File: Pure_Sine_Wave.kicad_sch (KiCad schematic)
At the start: 246 parts, among them J1 SOLAR, J10 Conn_01x01_Female, J11 Conn_01x01_Female, J12 Conn_01x01_Female, J13 Conn_01x01_Female, J14 Conn_01x01_Female, J15 Conn_01x01_Female, J16 Conn_01x01_Female, J17 Conn_01x01_Female, J18 Conn_01x01_Female, J19 Conn_01x01_Female, J2 Conn_01x01_Female, J20 Conn_01x01_Female, J21 Conn_01x01_Female, J22 Conn_01x01_Female, J23 Conn_01x01_Female, J24 Conn_01x01_Female, J25 Conn_01x01_Female, J26 Conn_01x01_Female, J27 Conn_01x01_Female, J28 Conn_01x01_Female, J29 Conn_01x01_Female, J3 Conn_01x01_Female, J30 Conn_01x01_Female, J31 Conn_01x01_Female, J32 Conn_01x01_Female, J33 Conn_01x01_Female, J34 Conn_01x01_Female, J36 FAN, J38 I2C_CON, J4 Conn_01x01_Female, J5 Conn_01x01_Female, J6 Conn_01x01_Female, J7 Conn_01x01_Female, J8 BATT, J9 USB_OTG, Q1 CSD19505, Q2 CSD19505, Q3 CSD19505, Q4 Si2306, Q5 2N3904, Q6 2N3904, Q7 PMOS-100V-78A, Q8 PMOS-100V-78A, Q9 Si2306, SW1 RIGHT, SW2 LEFT, SW3 BACK, SW4 SELECT, U1 ACS712-30A, U10 ADS1015, U11 NUP4202, U12 PCF8574, U2 B1212, U3 AMS1117-5.0, U4 AMS1117-3.3, U5 XL7005A, U6 XL7005A, U7 IR2104, U8 ESP32-WROOM-32, U9 CH340C

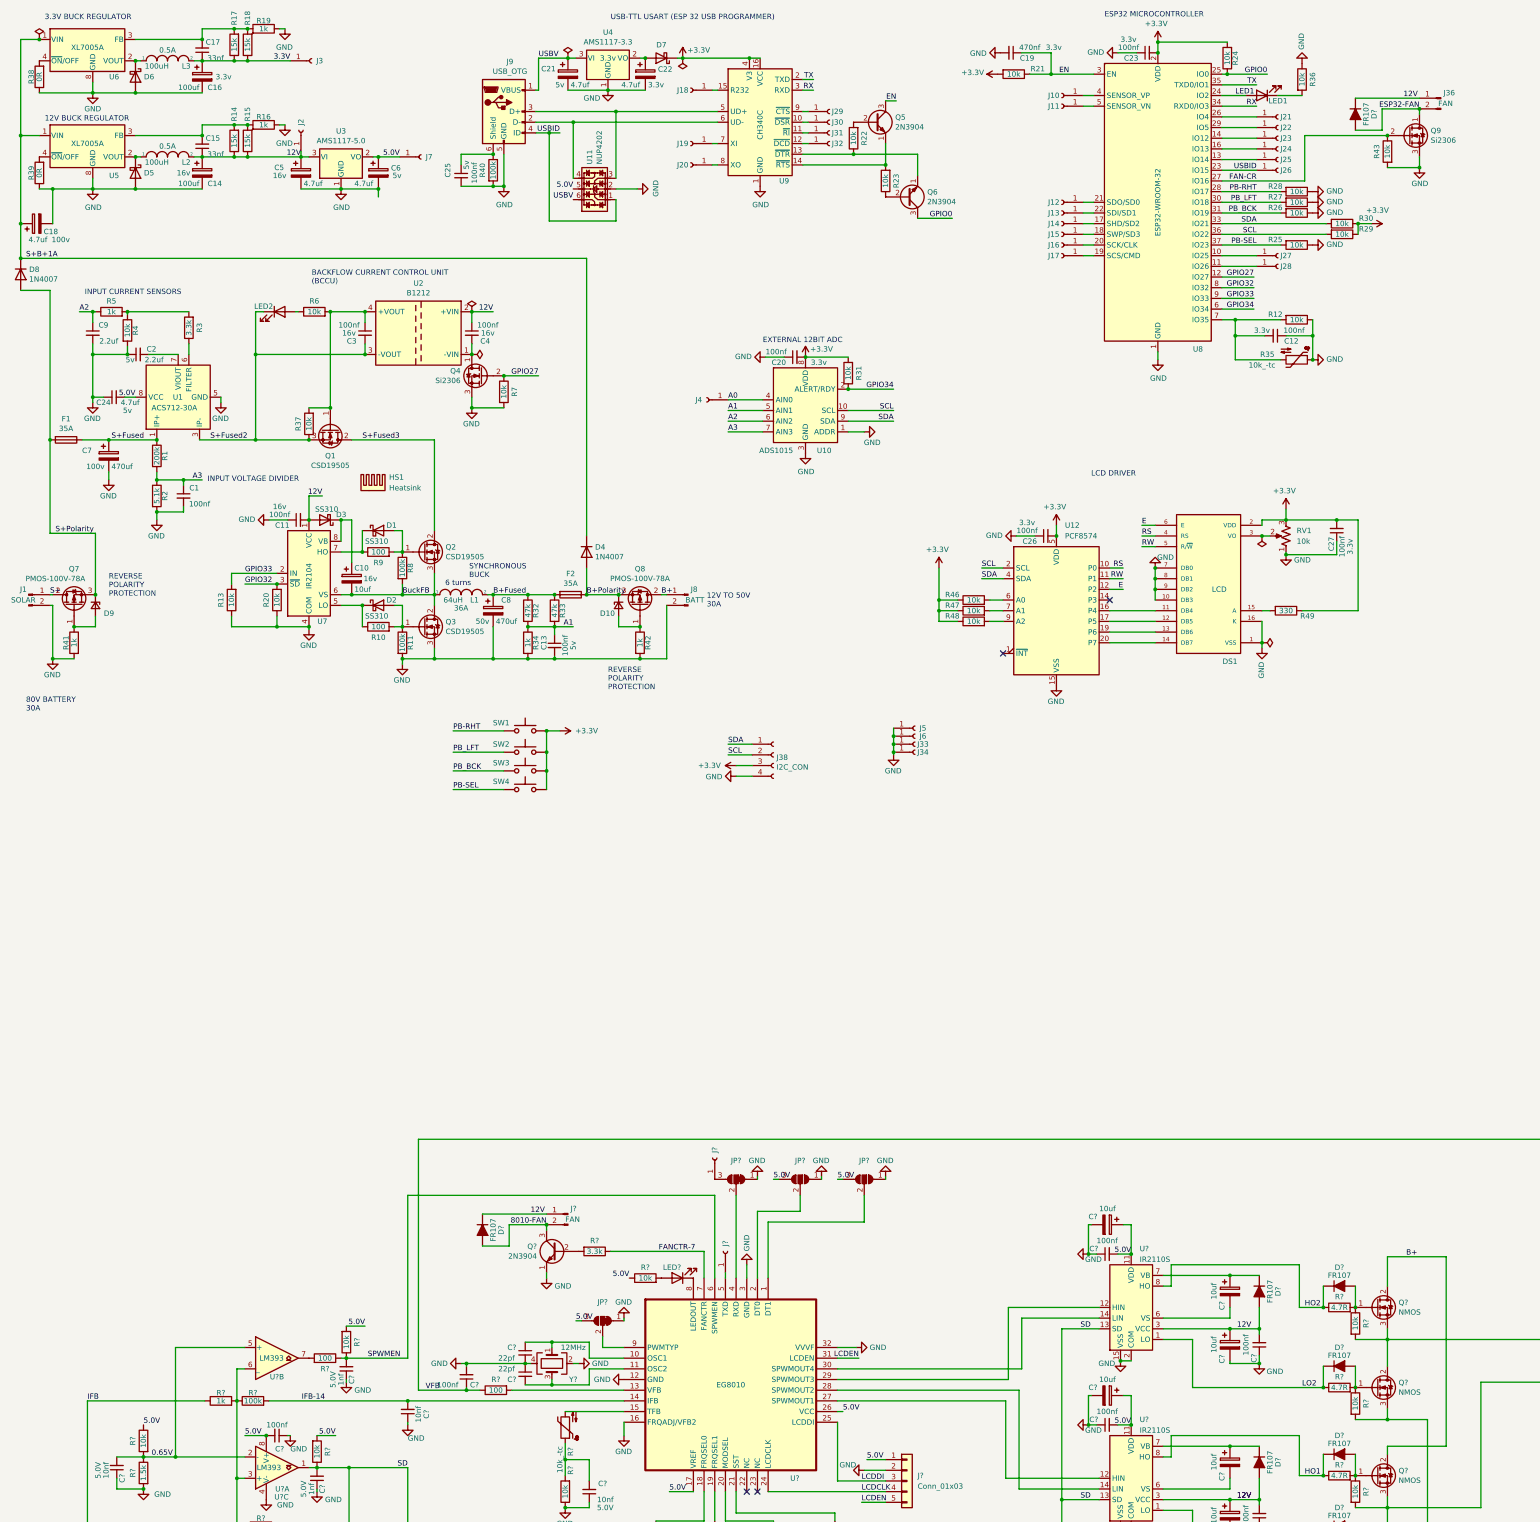
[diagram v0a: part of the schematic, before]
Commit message: Updated schematic to match changes form charge controller Added simulation for MOSFET heat predictions.
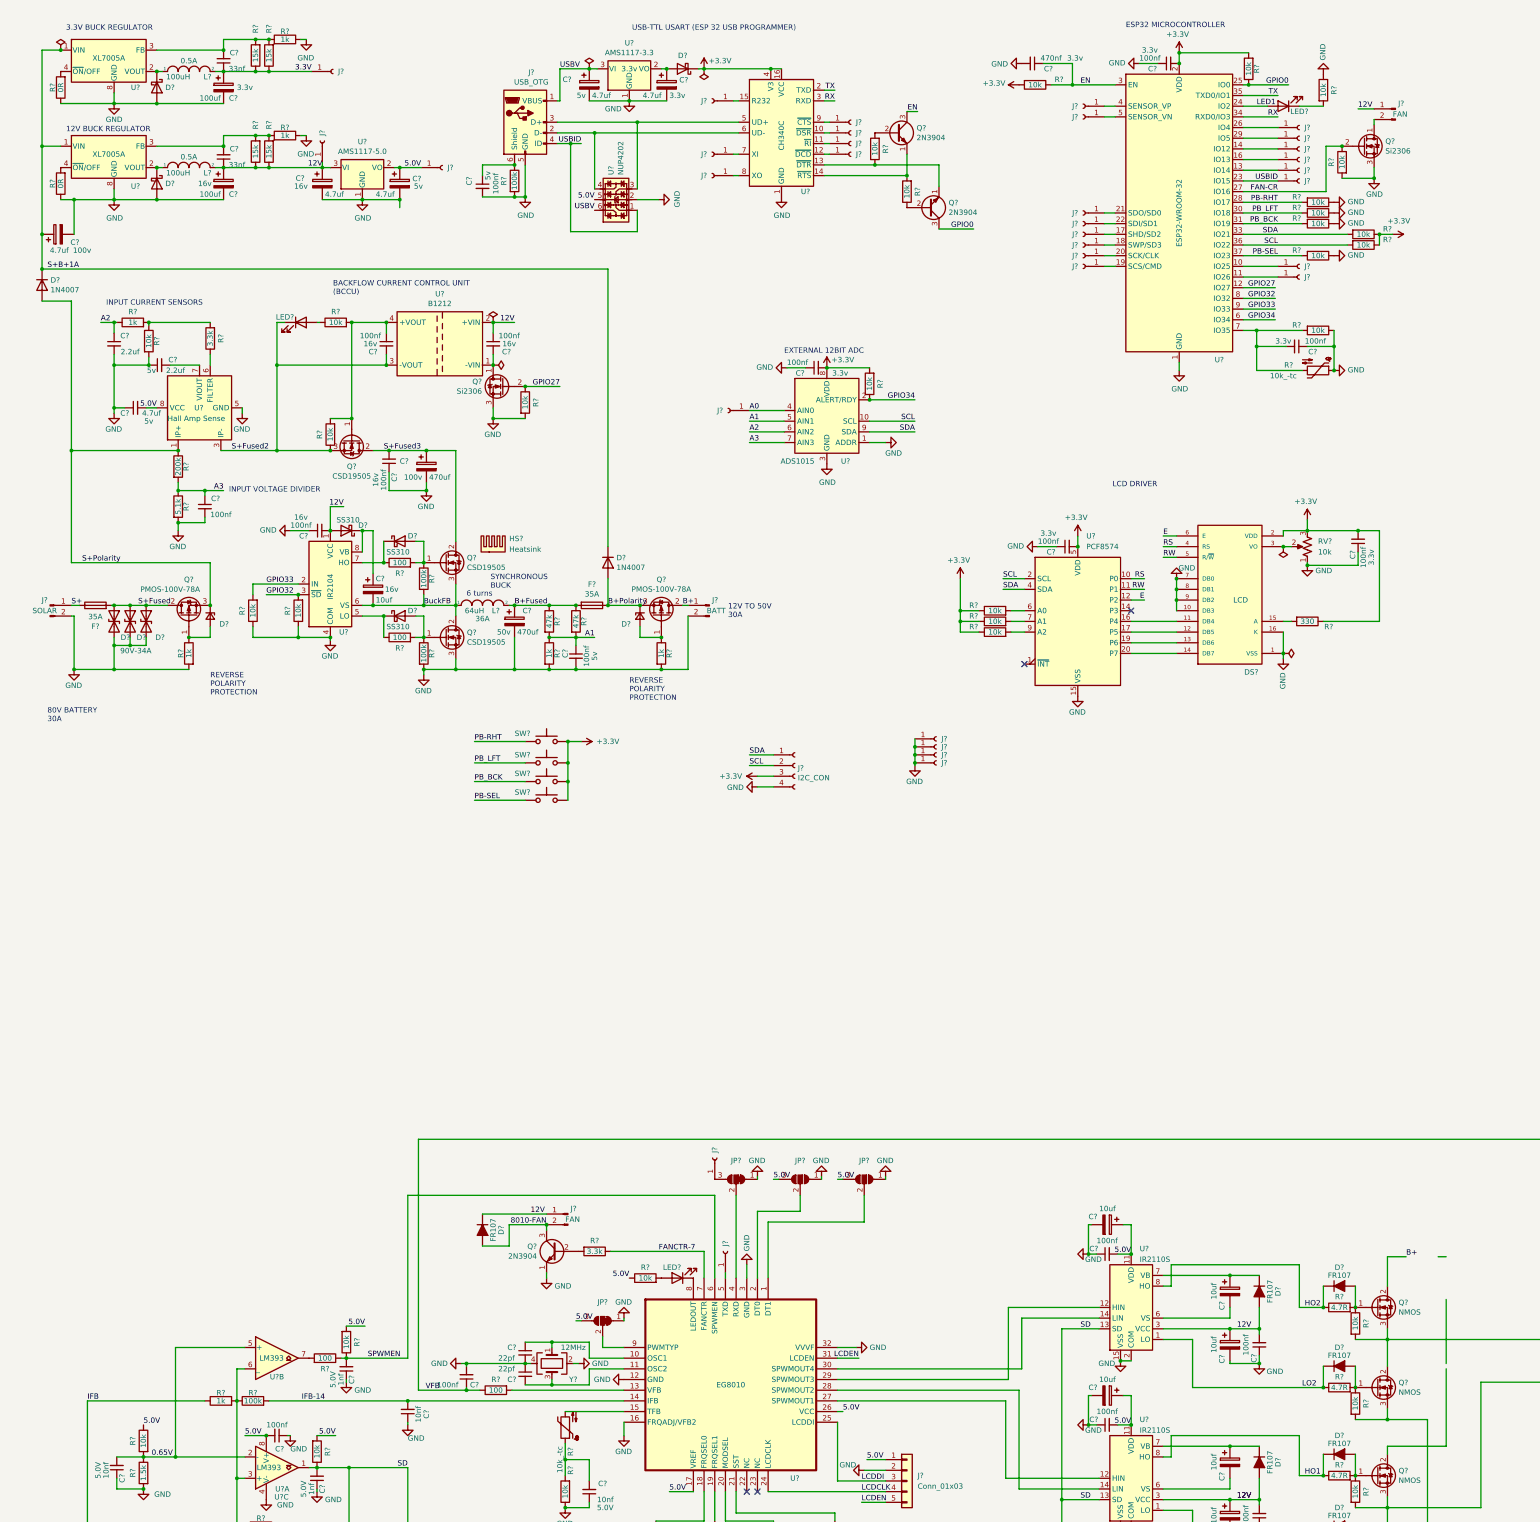
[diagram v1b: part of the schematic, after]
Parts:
- removed C1, C11, C12, C13, C20, C23, C25, C26, C27, C3, C4: 100nf, Capacitor_SMD:C_0805_2012Metric, symbol Device:C_Small
- removed C10: 10uf, Capacitor_SMD:C_0805_2012Metric, symbol Device:C_Polarized
- removed C14, C16: 100uf, Capacitor_SMD:CP_Elec_8x10, symbol Device:C_Polarized
- removed C15, C17: 33nf, Capacitor_SMD:C_0805_2012Metric, symbol Device:C_Small
- removed C18: 4.7uf, Capacitor_THT:CP_Radial_D10.0mm_P5.00mm, symbol Device:C_Polarized
- removed C19: 470nf, Capacitor_SMD:C_0805_2012Metric, symbol Device:C_Small
- removed C2, C9: 2.2uf, Capacitor_SMD:C_0805_2012Metric, symbol Device:C_Small
- removed C21, C22, C5, C6: 4.7uf, Capacitor_SMD:C_0805_2012Metric, symbol Device:C_Polarized
- removed C24: 4.7uf, Capacitor_SMD:C_0805_2012Metric, symbol Device:C_Small
- removed C7, C8: 470uf, Capacitor_THT:CP_Axial_L30.0mm_D18.0mm_P35.00mm_Horizontal, symbol Device:C_Polarized
- removed D1, D2, D3, D5, D6, D7: SS310, Diode_SMD:D_SMA, symbol Device:D_Schottky
- removed D10, D9: D_Zener_Small, Diode_SMD:D_MiniMELF_Handsoldering, symbol Device:D_Zener_Small
- removed D4, D8: 1N4007, Diode_SMD:D_SMA, symbol Diode:1N4007
- removed D?: FR107, Diode_SMD:D_SOD-123, symbol Device:D_Filled
- removed DS1: LCD, LCD:LCD_LCM-S01602DTR_A, symbol LCM-S01602DTR_A:LCM-S01602DTR/A
- removed F1, F2: 35A, Fuse:Fuseholder_Blade_Mini_Keystone_3568, symbol Device:Fuse
- removed HS1: Heatsink, Heatsink:Heatsink_Stonecold_HS-132_32x14mm_2xFixation1.5mm, symbol Mechanical:Heatsink
- removed J1: SOLAR, Phoenix_10.16_terminal_1709681:Phoenix_10.16_terminal_1709681, symbol Connector:Conn_01x02_Male
- removed J10, J11, J12, J13, J14, J15, J16, J17, J18, J19, J2, J20, J21, J22, J23, J24, J25, J26, J27, J28, J29, J3, J30, J31, J32, J33, J34, J4, J5, J6, J7: Conn_01x01_Female, TestPoint:TestPoint_Loop_D3.50mm_Drill0.9mm_Beaded, symbol Connector:Conn_01x01_Female
- removed J36: FAN, Phoenix_10.16_terminal_1709681:Phoenix_10.16_terminal_1709681, symbol Connector:Conn_01x02_Male
- removed J38: I2C_CON, Connector_PinHeader_2.54mm:PinHeader_1x04_P2.54mm_Vertical, symbol Connector:Conn_01x04_Female
- removed J8: BATT, Phoenix_10.16_terminal_1709681:Phoenix_10.16_terminal_1709681, symbol Connector:Conn_01x02_Male
- removed J9: USB_OTG, Connector_USB:USB_Micro-AB_Molex_47590-0001, symbol Connector:USB_B_Micro
- removed L1: 64uH, Inductor_THT:L_Axial_L30.0mm_D8.0mm_P35.56mm_Horizontal_Fastron_77A, symbol pspice:INDUCTOR
- removed L2, L3: 100uH, Inductor_SMD:L_Taiyo-Yuden_NR-60xx_HandSoldering, symbol pspice:INDUCTOR
- removed LED1, LED2: LED, LED_SMD:LED_0805_2012Metric, symbol Device:LED
- removed Q1, Q2, Q3: CSD19505, Package_TO_SOT_THT:TO-220-3_Vertical, symbol Device:Q_NMOS_GDS
- removed Q4, Q9: Si2306, Package_TO_SOT_SMD:SOT-23, symbol Device:Q_NMOS_DGS
- removed Q5, Q6: 2N3904, Package_TO_SOT_SMD:SOT-23, symbol Transistor_BJT:2N3904
- removed Q7, Q8: PMOS-100V-78A, Package_TO_SOT_SMD:TO-252-2, symbol Device:Q_PMOS_GDS
- removed R1: 200k, Resistor_SMD:R_0805_2012Metric, symbol Device:R
- removed R10, R9: 100, Resistor_SMD:R_0805_2012Metric, symbol Device:R
- removed R11, R40, R8: 100k, Resistor_SMD:R_0805_2012Metric, symbol Device:R
- removed R12, R13, R20, R21, R22, R23, R24, R25, R26, R27, R28, R29, R30, R31, R36, R37, R4, R43, R46, R47, R48, R6, R7: 10k, Resistor_SMD:R_0805_2012Metric, symbol Device:R
- removed R14, R15, R17, R18: 15k, Resistor_SMD:R_0805_2012Metric, symbol Device:R
- removed R16, R19, R34, R41, R42, R5: 1k, Resistor_SMD:R_0805_2012Metric, symbol Device:R
- removed R2: 5.1k, Resistor_SMD:R_0805_2012Metric, symbol Device:R
- removed R3: 3.3k, Resistor_SMD:R_0805_2012Metric, symbol Device:R
- removed R32, R33: 47k, Resistor_SMD:R_0805_2012Metric, symbol Device:R
- removed R35: 10k_-tc, Connector_PinHeader_2.54mm:PinHeader_1x02_P2.54mm_Vertical, symbol Device:Thermistor_NTC
- removed R38, R39: 0R, Resistor_SMD:R_0603_1608Metric, symbol Device:R
- removed R49: 330, Resistor_SMD:R_0805_2012Metric, symbol Device:R
- removed RV1: 10k, Potentiometer_SMD:Potentiometer_Bourns_3314G_Vertical, symbol Device:R_Potentiometer_US
- removed SW1: RIGHT, Button_Switch_SMD:SW_SPST_EVQQ2, symbol Switch:SW_Push
- removed SW2: LEFT, Button_Switch_SMD:SW_SPST_EVQQ2, symbol Switch:SW_Push
- removed SW3: BACK, Button_Switch_SMD:SW_SPST_EVQQ2, symbol Switch:SW_Push
- removed SW4: SELECT, Button_Switch_SMD:SW_SPST_EVQQ2, symbol Switch:SW_Push
- removed U1: ACS712-30A, Package_SO:SOIC-8_3.9x4.9mm_P1.27mm, symbol Sensor_Current:ACS712xLCTR-30A
- removed U10: ADS1015, Package_SO:TSSOP-10_3x3mm_P0.5mm, symbol Analog_ADC:ADS1015IDGS
- removed U11: NUP4202, Package_TO_SOT_SMD:SOT-363_SC-70-6, symbol Power_Protection:NUP4202
- removed U12: PCF8574, Package_SO:SSOP-20_5.3x7.2mm_P0.65mm, symbol Interface_Expansion:PCF8574
- removed U2: B1212, Converter_DCDC:Converter_DCDC_muRata_CRE1xxxxxxSC_THT, symbol Regulator_Switching:CRE1S1212SC
- removed U3: AMS1117-5.0, Package_TO_SOT_SMD:SOT-223-3_TabPin2, symbol Regulator_Linear:AMS1117-3.3
- removed U4: AMS1117-3.3, Package_TO_SOT_SMD:SOT-223-3_TabPin2, symbol Regulator_Linear:AMS1117-3.3
- removed U5, U6: XL7005A, Package_SO:SOIC-8_3.9x4.9mm_P1.27mm, symbol Regulator_Switching:GL2576-3.3SF8DR
- removed U7: IR2104, Package_SO:SOIC-8_3.9x4.9mm_P1.27mm, symbol Driver_FET:IR2104
- removed U8: ESP32-WROOM-32, RF_Module:ESP32-WROOM-32, symbol RF_Module:ESP32-WROOM-32
- removed U9: CH340C, Package_SO:STC_SOP-16_3.9x9.9mm_P1.27mm, symbol Interface_USB:CH340G
- added C? (x4): 4.7uf, Capacitor_SMD:C_0805_2012Metric, symbol Device:C_Polarized
- added C?: 4.7uf, Capacitor_SMD:C_0805_2012Metric, symbol Device:C_Small
- added C? (x2): 33nf, Capacitor_SMD:C_0805_2012Metric, symbol Device:C_Small
- added C? (x2): 2.2uf, Capacitor_SMD:C_0805_2012Metric, symbol Device:C_Small
- added C? (x12): 100nf, Capacitor_SMD:C_0805_2012Metric, symbol Device:C_Small
- added C? (x2): 100uf, Capacitor_SMD:CP_Elec_8x10, symbol Device:C_Polarized
- added C?: 470nf, Capacitor_SMD:C_0805_2012Metric, symbol Device:C_Small
- added C?: 10uf, Capacitor_SMD:C_0805_2012Metric, symbol Device:C_Polarized
- added C? (x2): 470uf, Capacitor_THT:CP_Radial_D16.0mm_P7.50mm, symbol Device:C_Polarized
- added C?: 4.7uf, Capacitor_THT:CP_Radial_D10.0mm_P5.00mm, symbol Device:C_Polarized
- added D? (x2): 1N4007, Diode_SMD:D_SMA, symbol Diode:1N4007
- added D?: 90V-34A, Diode_SMD:D_SMC-RM10_Universal_Handsoldering, symbol Device:D_TVS
- added D? (x2): D_Zener_Small, Diode_SMD:D_MiniMELF, symbol Device:D_Zener_Small
- added D? (x6): SS310, Diode_SMD:D_SMA, symbol Device:D_Schottky
- added D? (x2): 120V-26A, Diode_SMD:D_SMC-RM10_Universal_Handsoldering, symbol Device:D_TVS
- added DS?: LCD, LCD:LCD_LCM-S01602DTR_A, symbol LCM-S01602DTR_A:LCM-S01602DTR/A
- added F? (x2): 35A, Fuse:Fuseholder_Blade_Mini_Keystone_3568, symbol Device:Fuse
- added HS?: Heatsink, Heatsink:Heatsink_Stonecold_HS-132_32x14mm_2xFixation1.5mm, symbol Mechanical:Heatsink
- added J? (x31): Conn_01x01_Female, TestPoint:TestPoint_Loop_D3.50mm_Drill0.9mm_Beaded, symbol Connector:Conn_01x01_Female
- added J?: USB_OTG, Connector_USB:USB_Micro-AB_Molex_47590-0001, symbol Connector:USB_B_Micro
- added J?: I2C_CON, Connector_PinHeader_2.54mm:PinHeader_1x04_P2.54mm_Vertical, symbol Connector:Conn_01x04_Female
- added J?: SOLAR, Phoenix_10.16_terminal_1709681:Phoenix_10.16_terminal_1709681, symbol Connector:Conn_01x02_Male
- added J?: FAN, Phoenix_10.16_terminal_1709681:Phoenix_10.16_terminal_1709681, symbol Connector:Conn_01x02_Male
- added J?: BATT, Phoenix_10.16_terminal_1709681:Phoenix_10.16_terminal_1709681, symbol Connector:Conn_01x02_Male
- added L?: 64uH, Inductor_THT:L_Axial_L30.0mm_D8.0mm_P35.56mm_Horizontal_Fastron_77A, symbol pspice:INDUCTOR
- added L? (x2): 100uH, Inductor_SMD:L_Taiyo-Yuden_NR-60xx_HandSoldering, symbol pspice:INDUCTOR
- added LED? (x2): LED, LED_SMD:LED_0805_2012Metric, symbol Device:LED
- added Q? (x3): CSD19505, Package_TO_SOT_THT:TO-220-3_Vertical, symbol Device:Q_NMOS_GDS
- added Q? (x2): Si2306, Package_TO_SOT_SMD:SOT-23, symbol Device:Q_NMOS_DGS
- added Q? (x2): PMOS-100V-78A, Package_TO_SOT_SMD:TO-252-2, symbol Device:Q_PMOS_GDS
- added Q? (x2): 2N3904, Package_TO_SOT_SMD:SOT-23, symbol Transistor_BJT:2N3904
- added R? (x2): 0R, Resistor_SMD:R_0603_1608Metric, symbol Device:R
- added R? (x23): 10k, Resistor_SMD:R_0805_2012Metric, symbol Device:R
- added R? (x6): 1k, Resistor_SMD:R_0805_2012Metric, symbol Device:R
- added R? (x4): 15k, Resistor_SMD:R_0805_2012Metric, symbol Device:R
- added R? (x3): 100k, Resistor_SMD:R_0805_2012Metric, symbol Device:R
- added R? (x2): 47k, Resistor_SMD:R_0805_2012Metric, symbol Device:R
- added R? (x2): 100, Resistor_SMD:R_0805_2012Metric, symbol Device:R
- added R?: 10k_-tc, Connector_PinHeader_2.54mm:PinHeader_1x02_P2.54mm_Vertical, symbol Device:Thermistor_NTC
- added R?: 3.3k, Resistor_SMD:R_0805_2012Metric, symbol Device:R
- added R?: 330, Resistor_SMD:R_0805_2012Metric, symbol Device:R
- added R?: 5.1k, Resistor_SMD:R_0805_2012Metric, symbol Device:R
- added R?: 200k, Resistor_SMD:R_0805_2012Metric, symbol Device:R
- added RV?: 10k, Potentiometer_SMD:Potentiometer_Bourns_3314G_Vertical, symbol Device:R_Potentiometer_US
- added SW?: BACK, Button_Switch_SMD:SW_SPST_EVQQ2, symbol Switch:SW_Push
- added SW?: LEFT, Button_Switch_SMD:SW_SPST_EVQQ2, symbol Switch:SW_Push
- added SW?: RIGHT, Button_Switch_SMD:SW_SPST_EVQQ2, symbol Switch:SW_Push
- added SW?: SELECT, Button_Switch_SMD:SW_SPST_EVQQ2, symbol Switch:SW_Push
- added U?: PCF8574, Package_SO:SSOP-20_5.3x7.2mm_P0.65mm, symbol Interface_Expansion:PCF8574
- added U? (x2): XL7005A, Package_SO:SOIC-8_3.9x4.9mm_P1.27mm, symbol Regulator_Switching:GL2576-3.3SF8DR
- added U?: AMS1117-3.3, Package_TO_SOT_SMD:SOT-223-3_TabPin2, symbol Regulator_Linear:AMS1117-3.3
- added U?: ADS1015, Package_SO:TSSOP-10_3x3mm_P0.5mm, symbol Analog_ADC:ADS1015IDGS
- added U?: AMS1117-5.0, Package_TO_SOT_SMD:SOT-223-3_TabPin2, symbol Regulator_Linear:AMS1117-3.3
- added U?: NUP4202, Package_TO_SOT_SMD:SOT-363_SC-70-6, symbol Power_Protection:NUP4202
- added U?: CH340C, Package_SO:STC_SOP-16_3.9x9.9mm_P1.27mm, symbol Interface_USB:CH340G
- added U?: IR2104, Package_SO:SOIC-8_3.9x4.9mm_P1.27mm, symbol Driver_FET:IR2104
- added U?: ESP32-WROOM-32, RF_Module:ESP32-WROOM-32, symbol RF_Module:ESP32-WROOM-32
- added U?: Hall Amp Sense, Package_SO:SOIC-8_3.9x4.9mm_P1.27mm, symbol Sensor_Current:ACS712xLCTR-30A
- added U?: B1212, Converter_DCDC:Converter_DCDC_muRata_CRE1xxxxxxSC_THT, symbol Regulator_Switching:CRE1S1212SC
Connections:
- net +3.3VA: now also C?.2, C?.2, C?.2, C?.2, D?.1 (K), DS?.2 (VDD), J?.3 (Pin_3), R?.1, R?.1, R?.1, R?.1, R?.1, R?.1, R?.2, R?.2, R?.2, RV?.3, SW?.2, SW?.2, SW?.2, SW?.2, U?.16 (VCC), U?.2 (VDD), U?.4 (V3), U?.5 (VDD), U?.8 (VDD)
- net 12V: now also C?.1, C?.1, C?.1, C?.1, C?.2, D?.2 (A), J?.1 (Pin_1), J?.1 (Pin_1), L?.2, R?.1, R?.1, U?.1 (VCC), U?.2 (+VIN), U?.3 (VI)
- net 3.3V: now also C?.1, C?.1, J?.1 (Pin_1), L?.2, R?.1, R?.1
- net 5.0V: now also C?.1, C?.2, J?.1 (Pin_1), U?.2 (VO), U?.5, U?.8 (VCC)
- net A0: now also J?.1 (Pin_1), U?.4 (AIN0)
- net A1: now also C?.1, R?.1, R?.2, R?.2, U?.5 (AIN1)
- net A2: now also C?.1, R?.1, U?.6 (AIN2)
- net A3: now also C?.1, R?.1, R?.2, U?.7 (AIN3)
- net B+: now also J?.1 (Pin_1), Q?.2 (D); no longer Q?.2 (D)
- net B+Fused: now also C?.1, F?.2, L?.2, R?.1, R?.1
- net B+Polarity: now also D?.1 (K), D?.2 (A), F?.1, Q?.3 (S)
- net BuckFB: now also C?.2, L?.1, Q?.2 (D), Q?.3 (S), R?.2, U?.6 (VS)
- net E: now also DS?.6 (E), U?.12 (P2)
- net EN: now also C?.1, Q?.3 (C), R?.1, U?.3 (EN)
- net FAN-CR: now also Q?.2 (G), R?.1, U?.27 (IO16)
- net GND: now also C?.1, C?.1, C?.1, C?.1, C?.1, C?.1, C?.1, C?.1, C?.1, C?.2, C?.2, C?.2, C?.2, C?.2, C?.2, C?.2, C?.2, C?.2, C?.2, C?.2, C?.2, C?.2, C?.2, D?.2 (A), D?.2 (A), D?.2 (A2), D?.2 (A2), D?.2 (A2), DS?.1 (VSS), DS?.10 (DB3), DS?.16 (K), DS?.7 (DB0), DS?.8 (DB1), DS?.9 (DB2), J?.1 (Pin_1), J?.1 (Pin_1), J?.1 (Pin_1), J?.1 (Pin_1), J?.2 (Pin_2), J?.2 (Pin_2), J?.4 (Pin_4), J?.5 (GND), Q?.3 (S), Q?.3 (S), Q?.3 (S), R?.1, R?.1, R?.1, R?.1, R?.1, R?.1, R?.1, R?.1, R?.1, R?.1, R?.1, R?.1, R?.1, R?.2, R?.2, R?.2, R?.2, R?.2, R?.2, R?.2, R?.2, R?.2, RV?.1, U?.1 (ADDR), U?.1 (GND), U?.1 (GND), U?.1 (GND), U?.1 (GND), U?.15 (GND), U?.15 (VSS), U?.2, U?.3 (GND), U?.38 (GND), U?.39 (GND), U?.4 (COM), U?.5 (GND), U?.5 (GND), U?.5 (GND), U?.6 (GND), U?.6 (GND), U?.7 (GND), U?.7 (GND), U?.8 (GND), U?.8 (GND)
- net GPIO0: now also Q?.3 (C), R?.1, U?.25 (IO0)
- net GPIO27: now also Q?.2 (G), R?.1, U?.12 (IO27)
- net GPIO32: now also R?.2, U?.3 (~{SD}), U?.8 (IO32)
- net GPIO33: now also R?.2, U?.2 (IN), U?.9 (IO33)
- net GPIO34: now also R?.1, U?.2 (ALERT/RDY), U?.6 (IO34)
- net LED1: now also LED?.2 (A), U?.24 (IO2)
- net PB-RHT: now also R?.2, SW?.1, U?.28 (IO17)
- net PB-SEL: now also R?.2, SW?.1, U?.37 (IO23)
- net PB_BCK: now also R?.2, SW?.1, U?.31 (IO19)
- net PB_LFT: now also R?.2, SW?.1, U?.30 (IO18)
- net RS: now also DS?.4 (RS), U?.10 (P0)
- net RW: now also DS?.5 (R/~{W}), U?.11 (P1)
- net RX: now also U?.3 (RXD), U?.34 (RXD0/IO3)
- net S+: now also F?.1, J?.1 (Pin_1)
- net S+B+1A: now also C?.1, D?.1 (K), D?.1 (K), U?.1 (VIN), U?.1 (VIN)
- net S+Fused: now also D?.1 (A1), D?.1 (A1), D?.1 (A1), F?.2, Q?.2 (D)
- net S+Fused2: now also C?.2, LED?.1 (K), Q?.3 (S), R?.1, U?.3 (-VOUT), U?.3 (IP-), U?.4 (IP-)
- net S+Fused3: now also C?.1, C?.2, Q?.2 (D), Q?.2 (D)
- net S+Polarity: now also D?.1 (K), D?.2 (A), Q?.3 (S), R?.1, U?.1 (IP+), U?.2 (IP+)
- net SCL: now also J?.2 (Pin_2), R?.2, U?.10 (SCL), U?.2 (SCL), U?.36 (IO22)
- net SDA: now also J?.1 (Pin_1), R?.2, U?.33 (IO21), U?.4 (SDA), U?.9 (SDA)
- net TX: now also U?.2 (TXD), U?.35 (TXD0/IO1)
- net USBID: now also J?.1 (Pin_1), J?.4 (ID), U?.1, U?.23 (IO15)
- net USBV: now also C?.1, J?.1 (VBUS), U?.3 (VI), U?.6
- new net: R?.2, U?.4 (~{ON}/OFF) (x2)
- new net: J?.1 (Pin_1), U?.20 (SCK/CLK)
- new net: DS?.11 (DB4), U?.16 (P4)
- new net: DS?.12 (DB5), U?.17 (P5)
- new net: DS?.13 (DB6), U?.19 (P6)
- new net: DS?.14 (DB7), U?.20 (P7)
- new net: R?.2, U?.6 (A0)
- new net: R?.2, U?.7 (A1)
- new net: R?.2, U?.9 (A2)
- new net: C?.1, D?.2 (A), U?.2 (VO)
- new net: J?.1 (Pin_1), U?.14 (IO12)
- new net: C?.2, R?.2, R?.2, R?.2, U?.3 (FB) (x2)
- new net: D?.2 (A), Q?.1 (G), R?.1 (x2)
- new net: D?.1 (K), L?.1, U?.2 (VOUT) (x2)
- new net: C?.1, Q?.1 (G), R?.2, R?.2, U?.4 (+VOUT)
- new net: LED?.1 (K), R?.2
- new net: J?.1 (Pin_1), U?.15 (R232)
- new net: D?.2 (A), Q?.1 (G), R?.1, R?.2 (x2)
- new net: Q?.1 (E), R?.1, U?.13 (~{DTR})
- new net: Q?.2 (B), R?.2
- new net: C?.2, U?.7 (VIOUT)
- new net: J?.1 (Pin_1), U?.18 (SWP/SD3)
- new net: C?.2, Q?.1 (D), U?.1 (-VIN)
- new net: C?.1, J?.6 (Shield), R?.1
- new net: Q?.2 (B), R?.1
- new net: J?.1 (Pin_1), U?.11 (IO26)
- new net: J?.2 (D-), U?.4, U?.6 (UD-)
- new net: J?.3 (D+), U?.3, U?.5 (UD+)
- new net: R?.1, R?.2, R?.2
- new net: J?.1 (Pin_1), U?.29 (IO5)
- new net: Q?.1 (E), R?.2, U?.14 (~{RTS})
- new net: LED?.2 (A), R?.1
- new net: J?.1 (Pin_1), U?.5 (SENSOR_VN)
- new net: D?.1 (K), R?.1, U?.7 (HO)
- new net: J?.1 (Pin_1), U?.22 (SDI/SD1)
- new net: J?.1 (Pin_1), U?.16 (IO13)
- new net: J?.2 (Pin_2), Q?.1 (D)
- new net: J?.1 (Pin_1), U?.7 (XI)
- new net: C?.2, R?.2, R?.2, U?.7 (IO35)
- new net: J?.1 (Pin_1), U?.10 (IO25)
- new net: J?.1 (Pin_1), U?.11 (~{RI})
- new net: D?.1 (K), R?.1, U?.5 (LO)
- new net: J?.1 (Pin_1), U?.4 (SENSOR_VP)
- new net: R?.1, U?.6 (FILTER)
- new net: J?.1 (Pin_1), U?.10 (~{DSR})
- new net: J?.1 (Pin_1), U?.12 (~{DCD})
- new net: J?.1 (Pin_1), U?.8 (XO)
- new net: J?.1 (Pin_1), U?.9 (~{CTS})
- new net: DS?.15 (A), R?.2
- new net: DS?.3 (VO), RV?.2
- new net: C?.1, D?.1 (K), U?.8 (VB)
- new net: J?.1 (Pin_1), U?.13 (IO14)
- new net: J?.1 (Pin_1), U?.17 (SHD/SD2)
- new net: J?.1 (Pin_1), U?.19 (SCS/CMD)
- new net: J?.1 (Pin_1), U?.21 (SDO/SD0)
- new net: J?.1 (Pin_1), U?.26 (IO4)
